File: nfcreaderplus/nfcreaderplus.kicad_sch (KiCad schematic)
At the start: 9 parts, among them J1 Conn_01x02, K1 G5Q-1A, U1 WeMos_D1_mini, U2 NFC_Reader_V3, U3 ULN2003

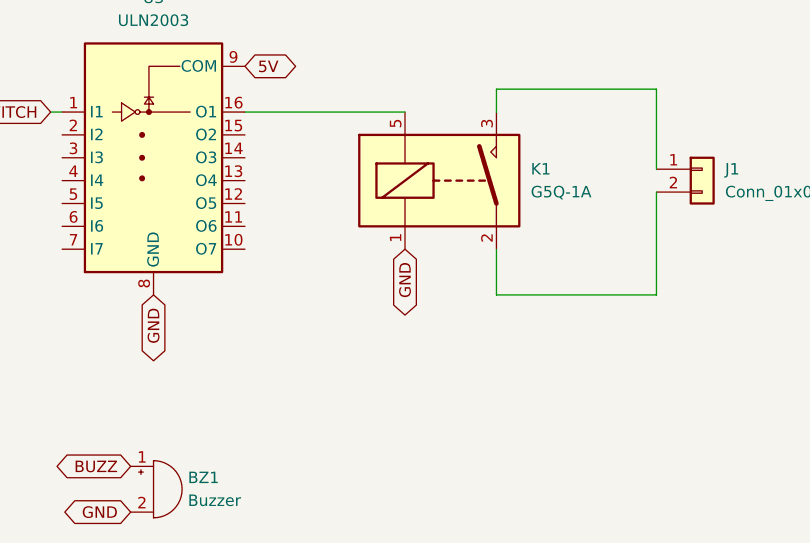
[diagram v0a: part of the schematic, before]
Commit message: relay driver is grounding, pass 5V through relay then
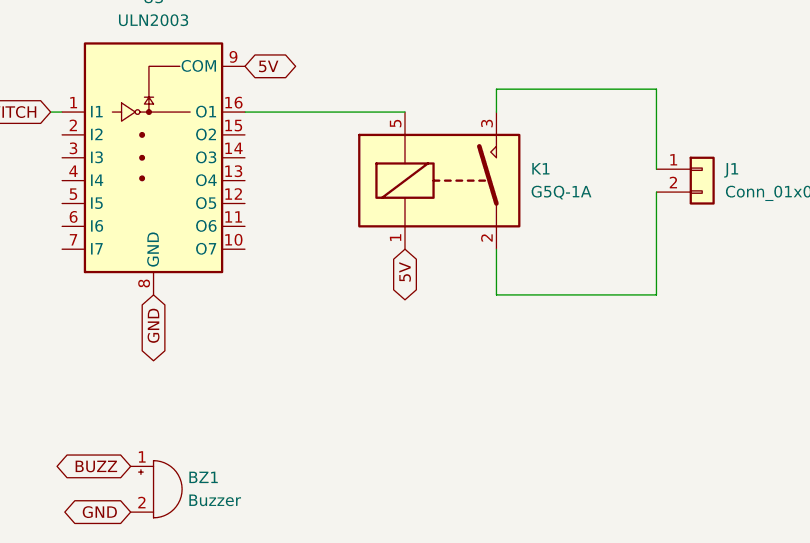
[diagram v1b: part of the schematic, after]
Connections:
- net 5V: now also K1.1
- net GND: no longer K1.1
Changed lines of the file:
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@@
     )
   )
-  (global_label "GND" (shape bidirectional) (at 162.56 142.24 270) (fields_autoplaced)
+  (global_label "5V" (shape bidirectional) (at 162.56 142.24 270) (fields_autoplaced)
     (effects (font (size 1.27 1.27)) (justify right))
-    (property "Intersheet References" "${INTERSHEET_REFS}" (id 0) (at 162.6394 148.5236 90)
+    (property "Intersheet References" "${INTERSHEET_REFS}" (id 0) (at 162.4806 146.9512 90)
       (effects (font (size 1.27 1.27)) (justify right) hide)
     )
